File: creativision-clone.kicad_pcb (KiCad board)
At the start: 2 copper layers, 208.8 x 99.7 mm, 105 parts, among them J1 Conn_01x10_Socket, J2 Conn_01x10_Socket, J3 Conn_01x07_Pin, J4 Conn_01x04_Socket, J5 RCJ-013, J6 RCJ-014, P1 Cartridge Slot, Q1 2n4401, SW1 Reset, SW2 Power Toggle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

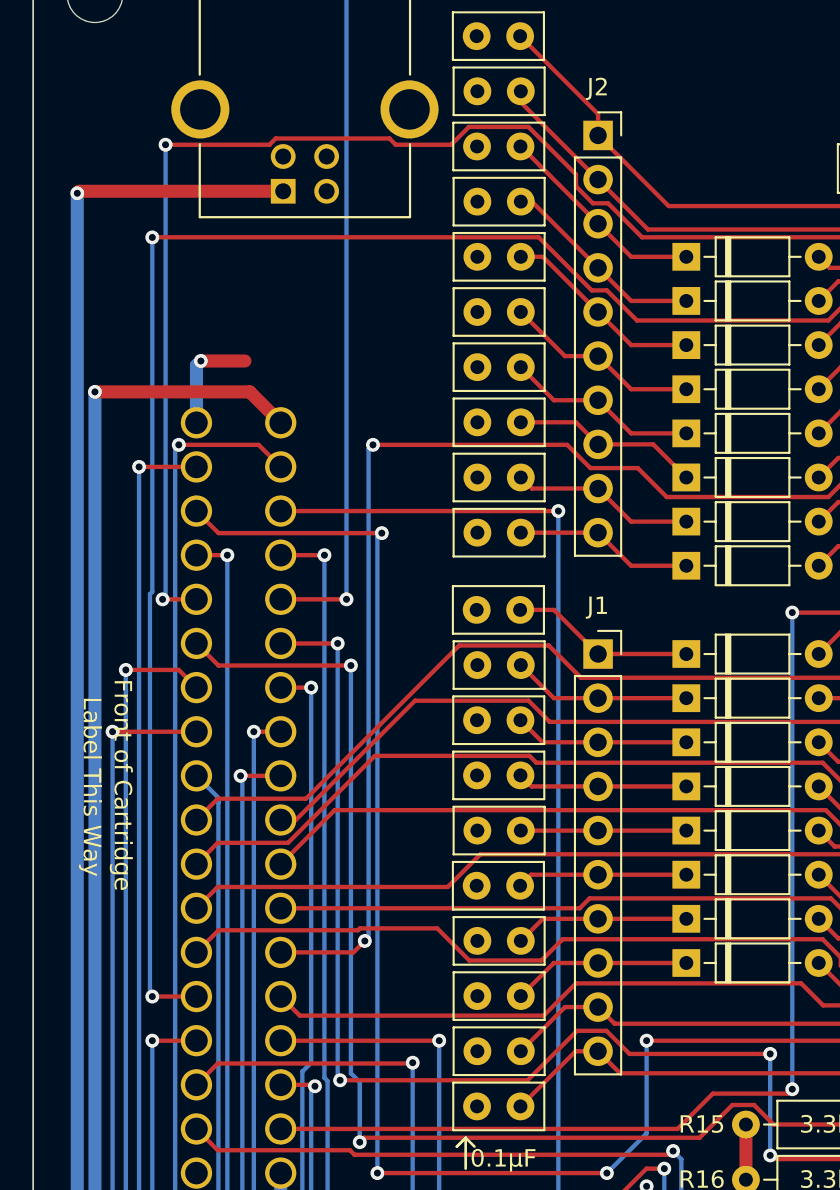
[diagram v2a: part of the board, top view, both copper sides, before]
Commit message: KiCad update, label PAx pins on headers
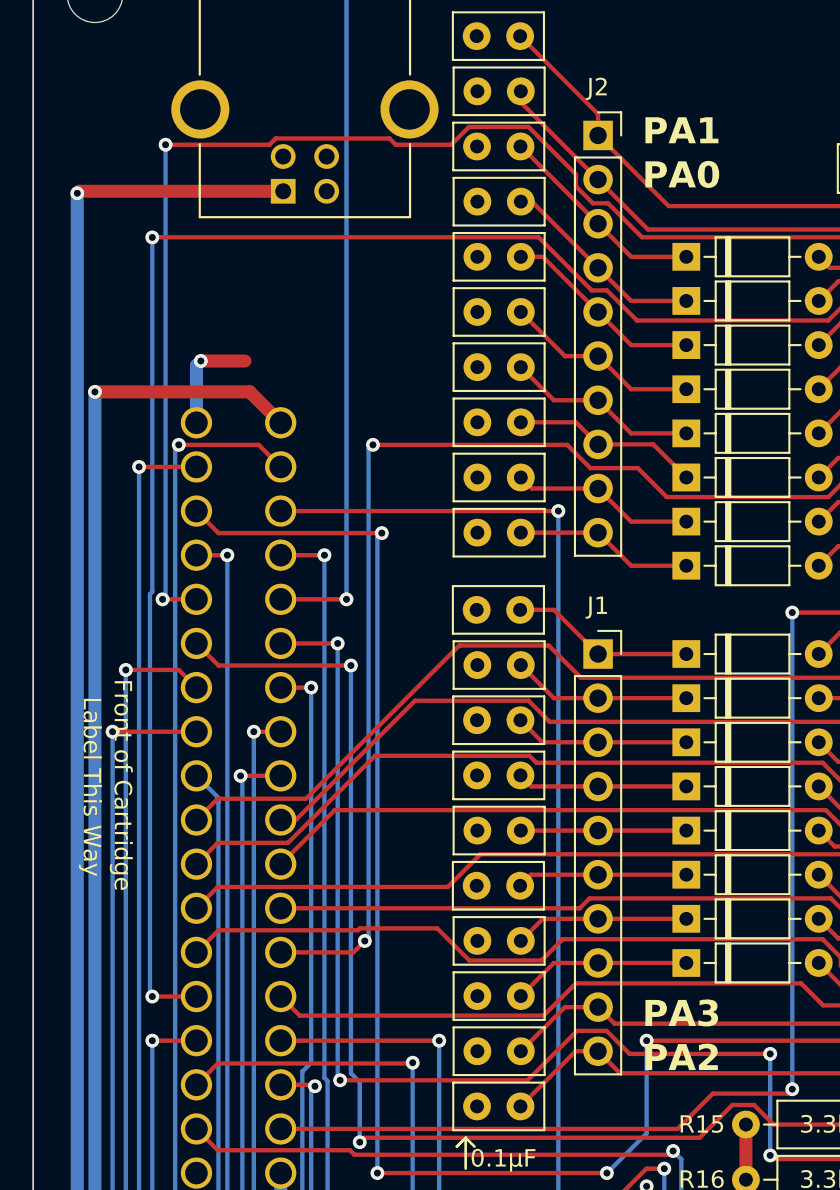
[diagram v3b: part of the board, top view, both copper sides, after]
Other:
- board text added: "PA0"
- board text added: "PA1"
- board text added: "PA2"
- board text added: "PA3"
